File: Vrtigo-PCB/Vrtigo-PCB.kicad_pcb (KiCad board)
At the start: 2 copper layers, 21.3 x 29.2 mm, 18 parts, among them CN1 PJ-320D, CN2 PJ-320D, Q1 2N3906, Q2 2N3906, Q3 2N3906, Q4 2N3906, Q5 2n3904, Q6 2n3904, Q7 2n3904, Q8 2n3904

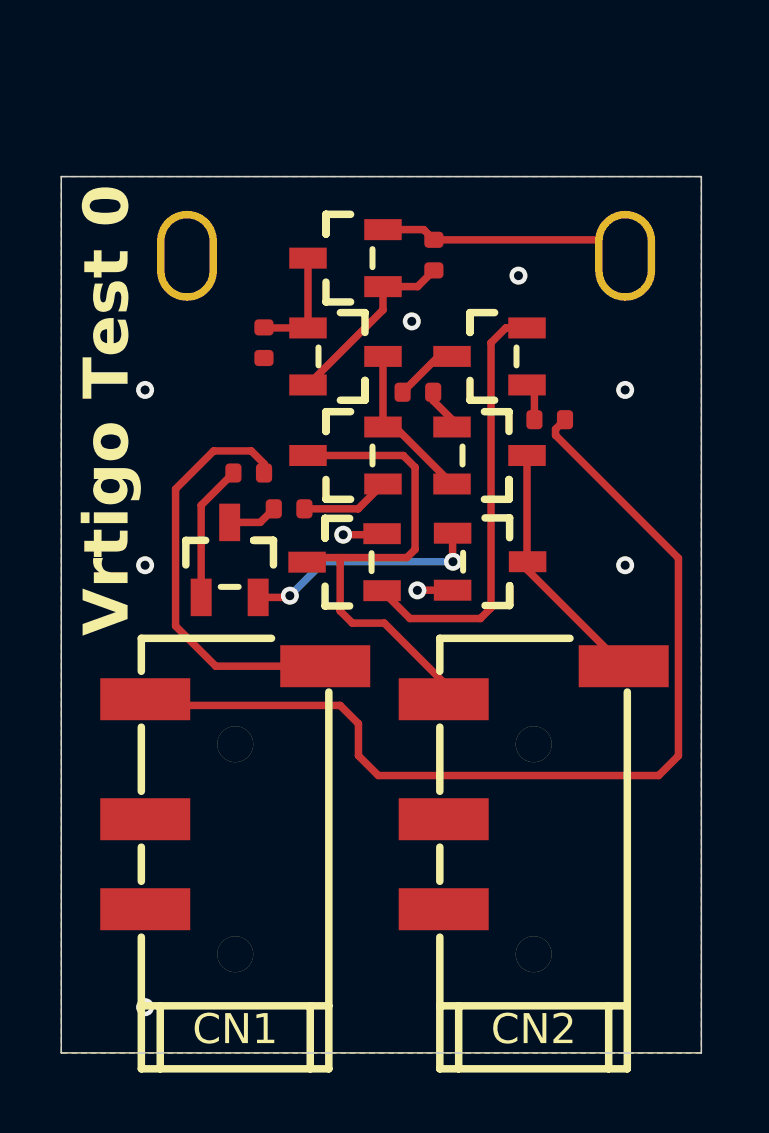
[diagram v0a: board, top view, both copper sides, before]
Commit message: - Improved PCB layout - Added PCB silkscreen
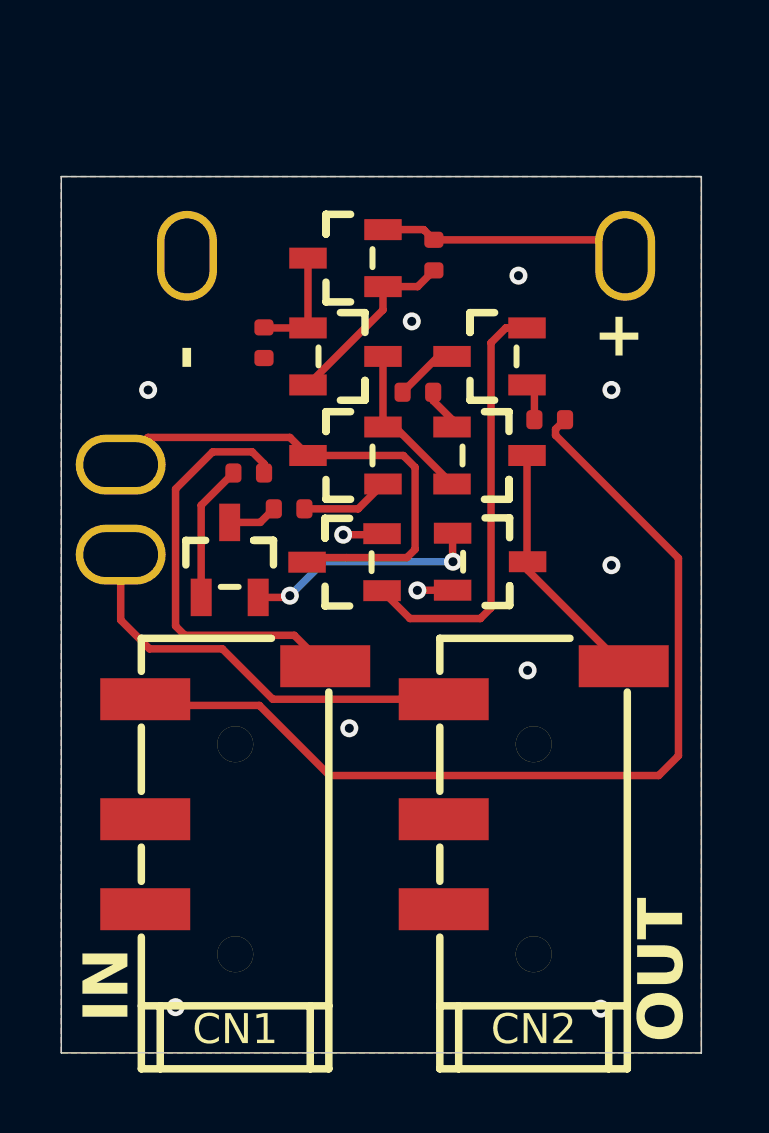
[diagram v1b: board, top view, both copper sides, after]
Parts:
- added TP3: ~, justPads_custom:2_3-1.5_2.5_1_1, F.Cu at (123.6, 96.2)
- added TP4: ~, justPads_custom:2_3-1.5_2.5_1_1, F.Cu at (123.6, 93.2)
- R1: value 220R -> 220R +-1%
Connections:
- Q3 pad 3: E1 -> Meter
- Q5 pad 3: E1 -> Meter
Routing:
- net Meter: track 0.00 -> 17.1 mm
- net E1: track 17.0 -> 14.6 mm
- net B: track 32.8 -> 32.1 mm
- net GND: vias 10 -> 12
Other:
- board text added: "+"
- board text added: "-"
- board text added: "IN"
- board text added: "MP-V-T.0.0 {dblquote}Vrtigo{dblquote}"
- board text added: "OUT"
- board text added: "Test Board Not For Resale"
- board text removed: "Vrtigo Test 0"
